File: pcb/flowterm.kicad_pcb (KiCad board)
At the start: 2 copper layers, 100 x 50 mm, 48 parts, among them J1 Vin, J10 Snapoff inner, J11 Prog, J12 Cool pump, J13 Fridge, J14 1W, J2 Flow1, J3 Flow2, J4 Flow3, J5 Flow4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

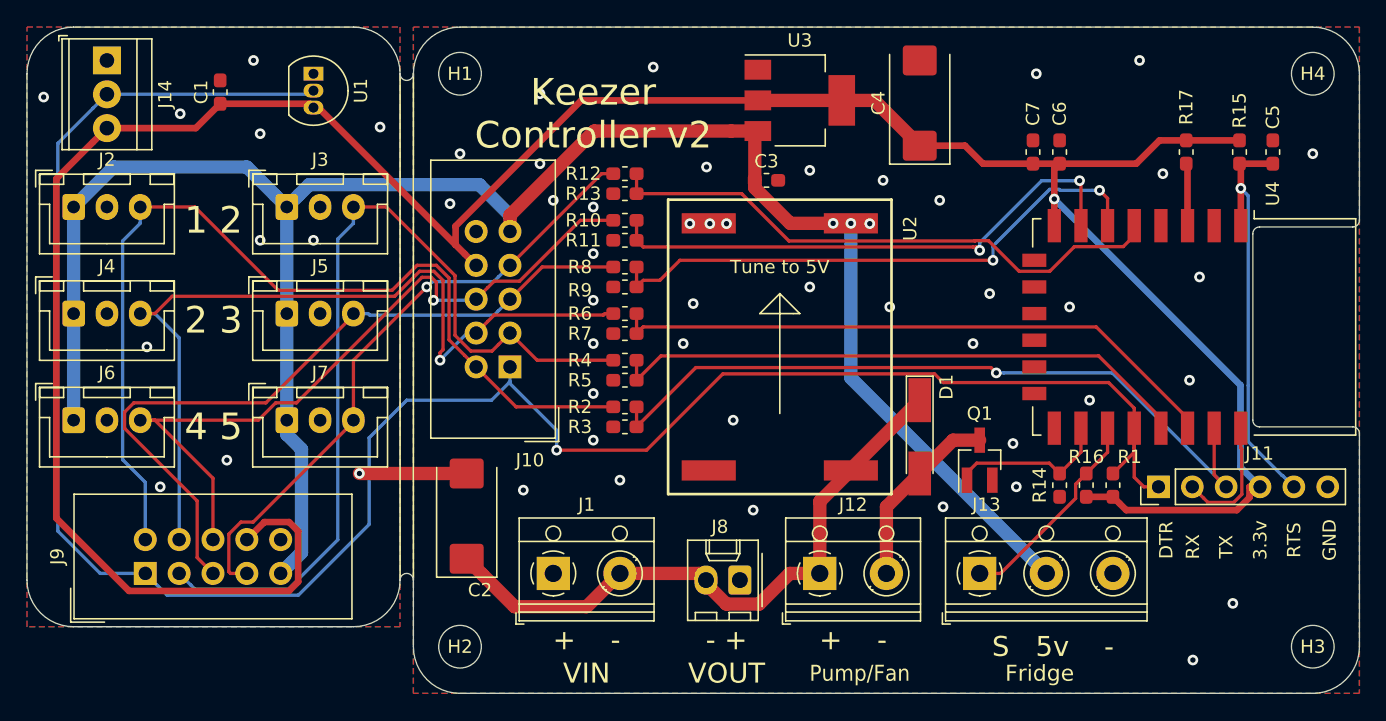
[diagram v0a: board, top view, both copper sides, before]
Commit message: PCB: fix silkscreen
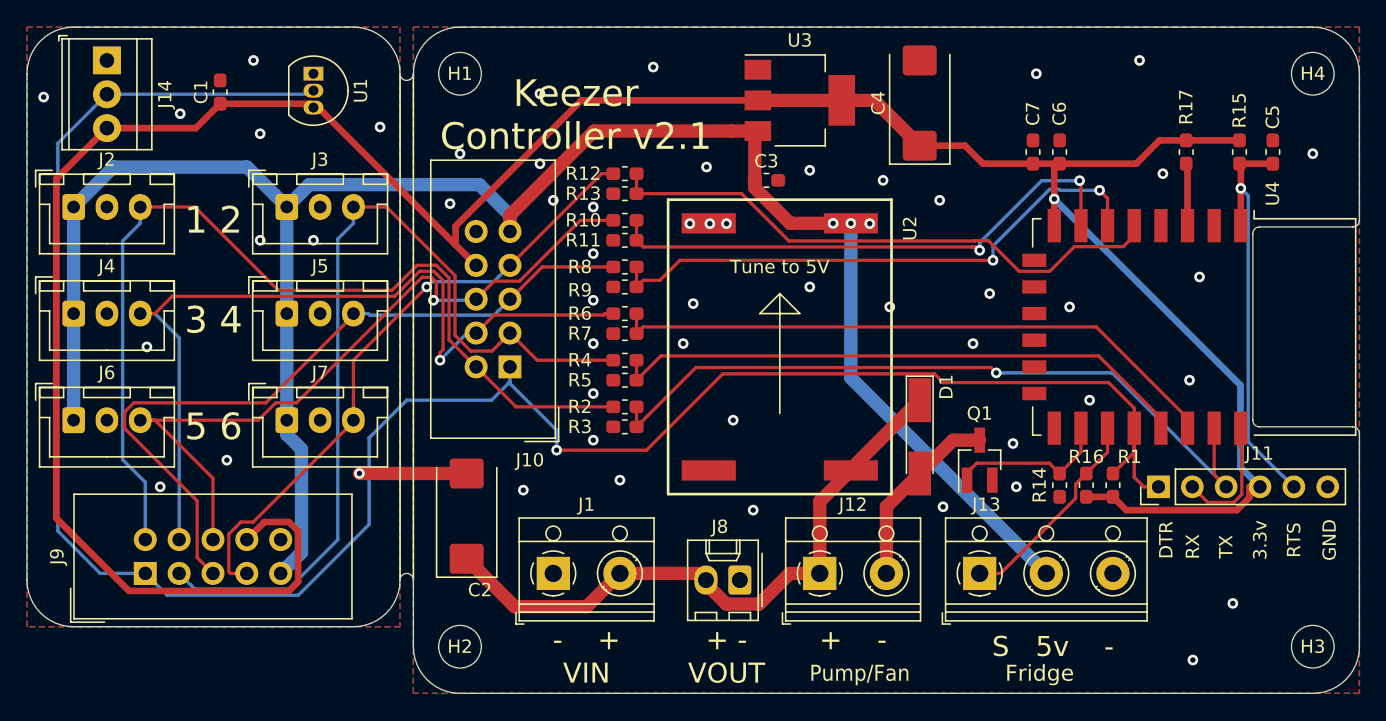
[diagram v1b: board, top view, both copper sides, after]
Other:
- board text added: "3 4"
- board text added: "5 6"
- board text added: "Keezer Controller v2.1"
- board text removed: "2 3"
- board text removed: "4 5"
- board text removed: "Keezer Controller v2"
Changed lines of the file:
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@@
-(kicad_pcb (version 20171130) (host pcbnew "(5.1.4)-1")
+(kicad_pcb (version 20171130) (host pcbnew "(5.1.4-0-10_14)")
   (general
     (thickness 1.6)
@@
     )
   )
-  (gr_text "Keezer \nController v2" (at 72.5 86.5) (layer F.SilkS)
+  (gr_text "Keezer \nController v2.1" (at 71.2 86.6) (layer F.SilkS)
     (effects (font (size 2 2) (thickness 0.4)))
   )
@@
   (gr_arc (start 122.5 95.5) (end 122.5 95) (angle -90) (layer Edge.Cuts) (width 0.05))
   (gr_arc (start 129.5 110.5) (end 130 110.5) (angle -90) (layer Edge.Cuts) (width 0.05))
-  (gr_text "4 5" (at 44 110) (layer F.SilkS)
+  (gr_text "5 6" (at 44 110) (layer F.SilkS)
     (effects (font (size 2 2) (thickness 0.4)))
   )
-  (gr_text "2 3" (at 44 102) (layer F.SilkS)
+  (gr_text "3 4" (at 44 102) (layer F.SilkS)
     (effects (font (size 2 2) (thickness 0.4)))
   )
@@
     (effects (font (size 1.5 1.5) (thickness 0.3)))
   )
-  (gr_text "- +" (at 82.5 126) (layer F.SilkS)
+  (gr_text "+ -" (at 82.5 126) (layer F.SilkS)
     (effects (font (size 1.5 1.5) (thickness 0.3)))
   )
-  (gr_text "+    -" (at 72 126) (layer F.SilkS)
+  (gr_text "-    +" (at 72 126) (layer F.SilkS)
     (effects (font (size 1.5 1.5) (thickness 0.3)))
   )
